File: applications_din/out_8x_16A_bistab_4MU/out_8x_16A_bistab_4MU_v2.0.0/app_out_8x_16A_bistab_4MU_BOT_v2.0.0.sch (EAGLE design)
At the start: 30 parts, among them IC1 ULN2803, IC2 ULN2803, K1 HFE20-1, K2 HFE20-1, K3 HFE20-1, K4 HFE20-1, K5 HFE20-1, K6 HFE20-1, K7 HFE20-1, K8 HFE20-1

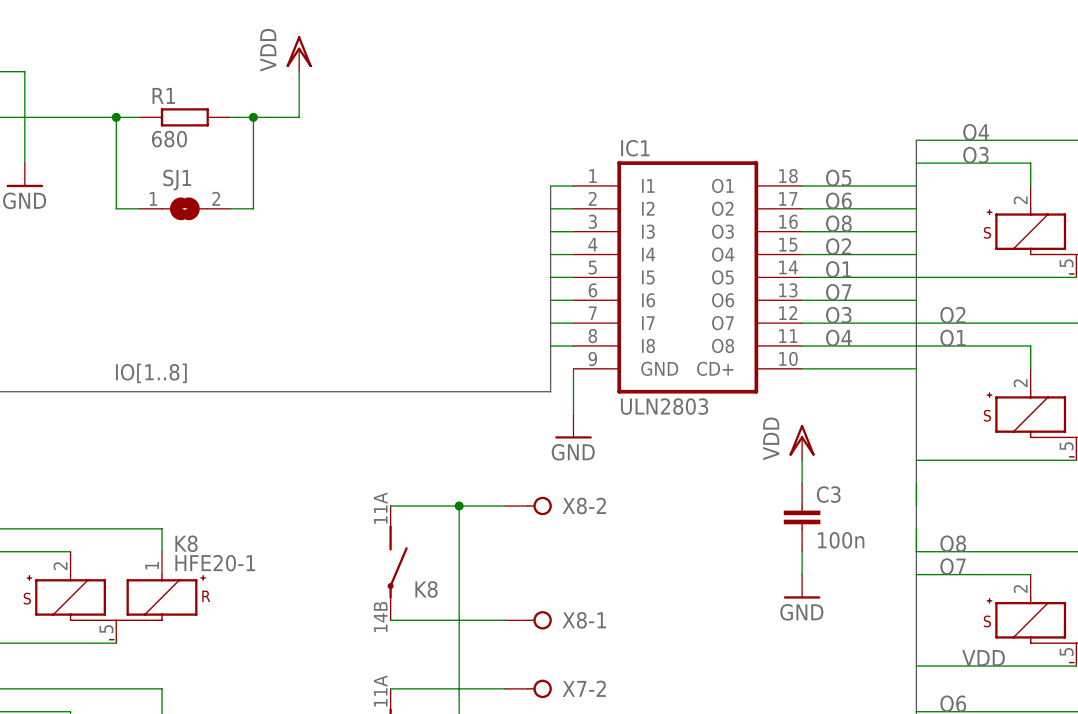
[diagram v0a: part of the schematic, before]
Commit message: [Application - out8 16A - bistable relay - 4TE - BOT] erc edited
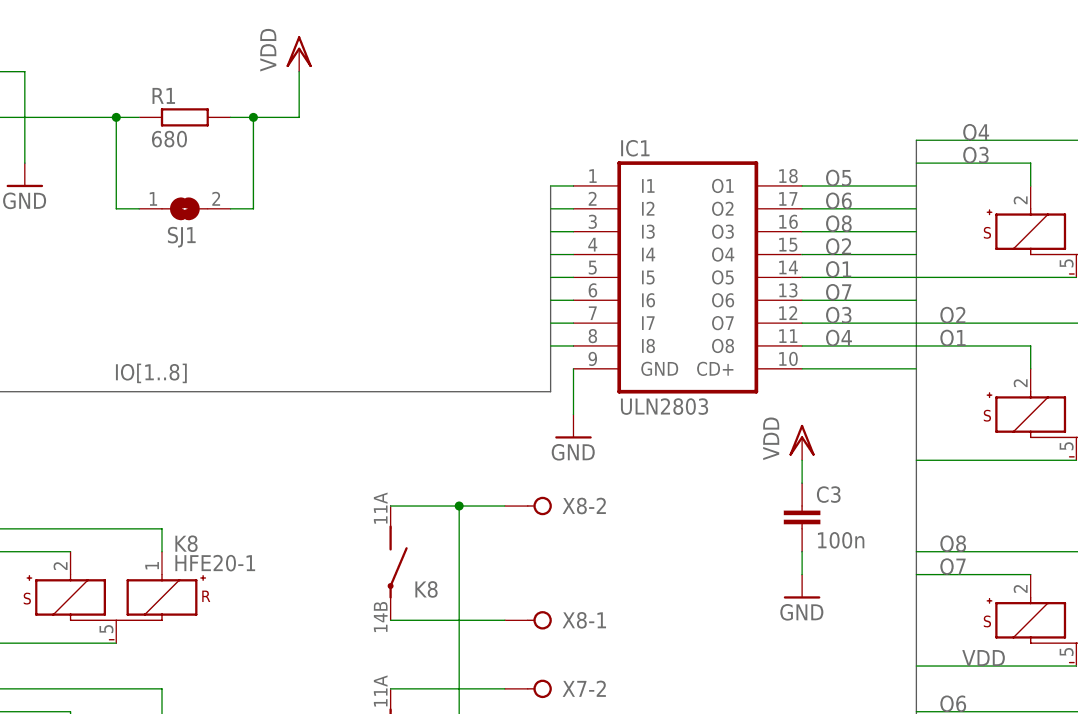
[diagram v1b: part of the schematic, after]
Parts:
- JP2, SJ1: value (none) -> A
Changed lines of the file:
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@@
 <part name="X7" library="con-wago-508" deviceset="W237-02P" device=""/>
 <part name="X8" library="con-wago-508" deviceset="W237-02P" device=""/>
-<part name="JP2" library="pinhead" deviceset="PINHD-2X13" device="_2.54-SMD"/>
+<part name="JP2" library="pinhead" deviceset="PINHD-2X13" device="_2.54-SMD" value="A"/>
 <part name="R1" library="rcl" deviceset="R-EU_" device="M1206" value="680"/>
 <part name="VDD3" library="supply1" deviceset="VDD" device=""/>
@@
 <part name="GND5" library="supply1" deviceset="GND" device=""/>
 <part name="C2" library="rcl" deviceset="CPOL-EU" device="E3.5-8" value="330µF/35V"/>
-<part name="SJ1" library="jumper" deviceset="SJ" device=""/>
+<part name="SJ1" library="jumper" deviceset="SJ" device="" value="A"/>
 <part name="VDD5" library="supply1" deviceset="VDD" device=""/>
 <part name="GND6" library="supply1" deviceset="GND" device=""/>
@@
 <instance part="X8" gate="-1" x="134.62" y="106.68" rot="R180"/>
 <instance part="X8" gate="-2" x="134.62" y="119.38" rot="R180"/>
-<instance part="JP2" gate="A" x="45.72" y="152.4"/>
+<instance part="JP2" gate="A" x="45.72" y="152.4" smashed="yes">
+<attribute name="NAME" x="39.37" y="170.815" size="1.778" layer="95"/>
+</instance>
 <instance part="R1" gate="G$1" x="93.98" y="162.56"/>
 <instance part="VDD3" gate="G$1" x="106.68" y="170.18"/>
@@
 <attribute name="VALUE" x="60.4774" y="18.923" size="1.778" layer="96" rot="R90"/>
 </instance>
-<instance part="SJ1" gate="1" x="93.98" y="152.4"/>
+<instance part="SJ1" gate="1" x="93.98" y="152.4" smashed="yes">
+<attribute name="NAME" x="91.948" y="148.59" size="1.778" layer="95"/>
+</instance>
 <instance part="VDD5" gate="G$1" x="38.1" y="86.36"/>
 <instance part="GND6" gate="1" x="38.1" y="68.58"/>
@@
 </segment>
 </bus>
-<bus name="B$1">
+<bus name="O[9..16],VDD">
 <segment>
 <wire x1="63.5" y1="116.84" x2="63.5" y2="40.64" width="0.762" layer="92"/>
 </segment>
 </bus>
-<bus name="B$2">
+<bus name="O[1..8],VDD">
 <segment>
 <wire x1="175.26" y1="160.02" x2="175.26" y2="81.28" width="0.762" layer="92"/>
@@
 <net name="O4" class="0">
 <segment>
-<wire x1="175.26" y1="121.92" x2="175.26" y2="119.38" width="0.1524" layer="91"/>
-</segment>
-<segment>
 <pinref part="K2" gate="G$1" pin="R+"/>
 <wire x1="198.12" y1="160.02" x2="198.12" y2="154.94" width="0.1524" layer="91"/>
@@
 </net>
 <net name="O1" class="0">
-<segment>
-<wire x1="175.26" y1="114.3" x2="175.26" y2="116.84" width="0.1524" layer="91"/>
-</segment>
 <segment>
 <wire x1="187.96" y1="137.16" x2="187.96" y2="134.62" width="0.1524" layer="91"/>
@@
 </sheet>
 </sheets>
+<errors>
+</errors>
 </schematic>
 </drawing>
